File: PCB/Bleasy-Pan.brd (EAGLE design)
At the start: 33.6 x 62.2 mm, 14 parts, among them IC1 ATMEGA328-PU, Q1 8 MHz

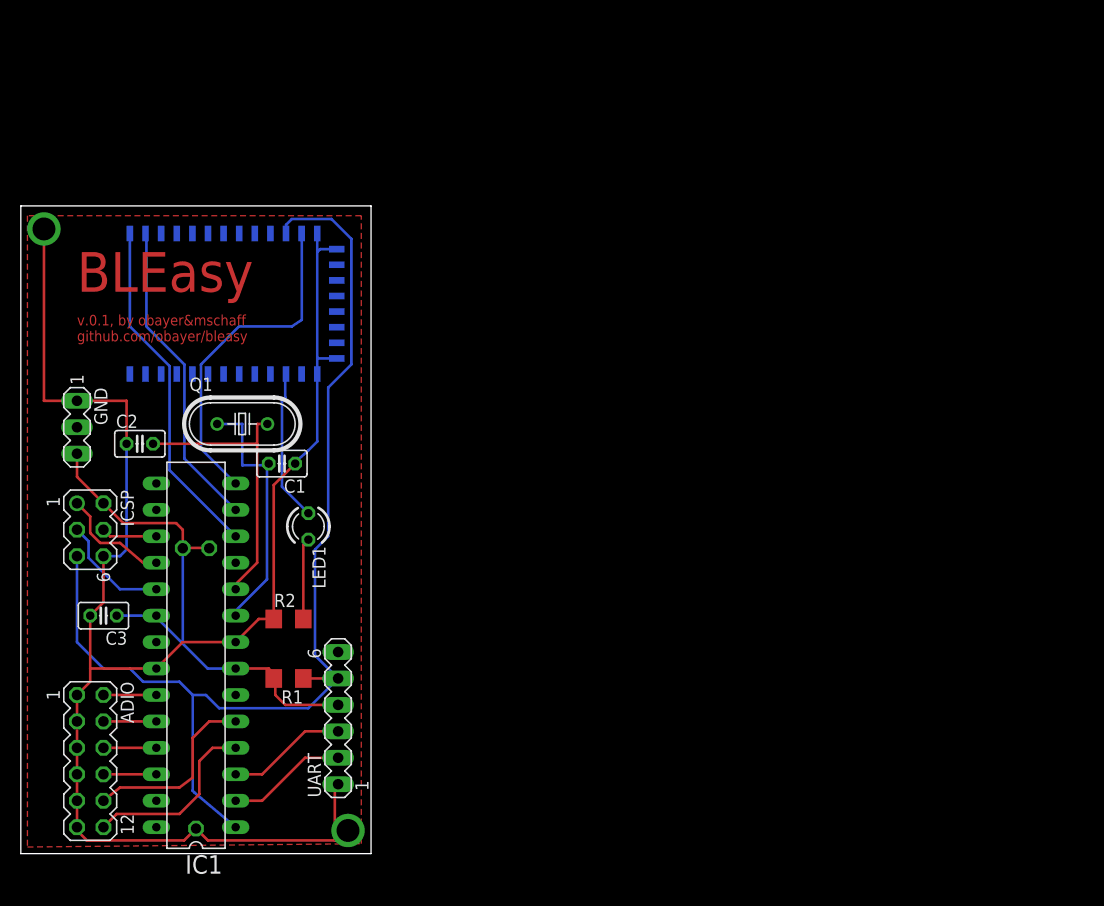
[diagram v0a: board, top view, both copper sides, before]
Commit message: feat(Panelize): Added panelized board.
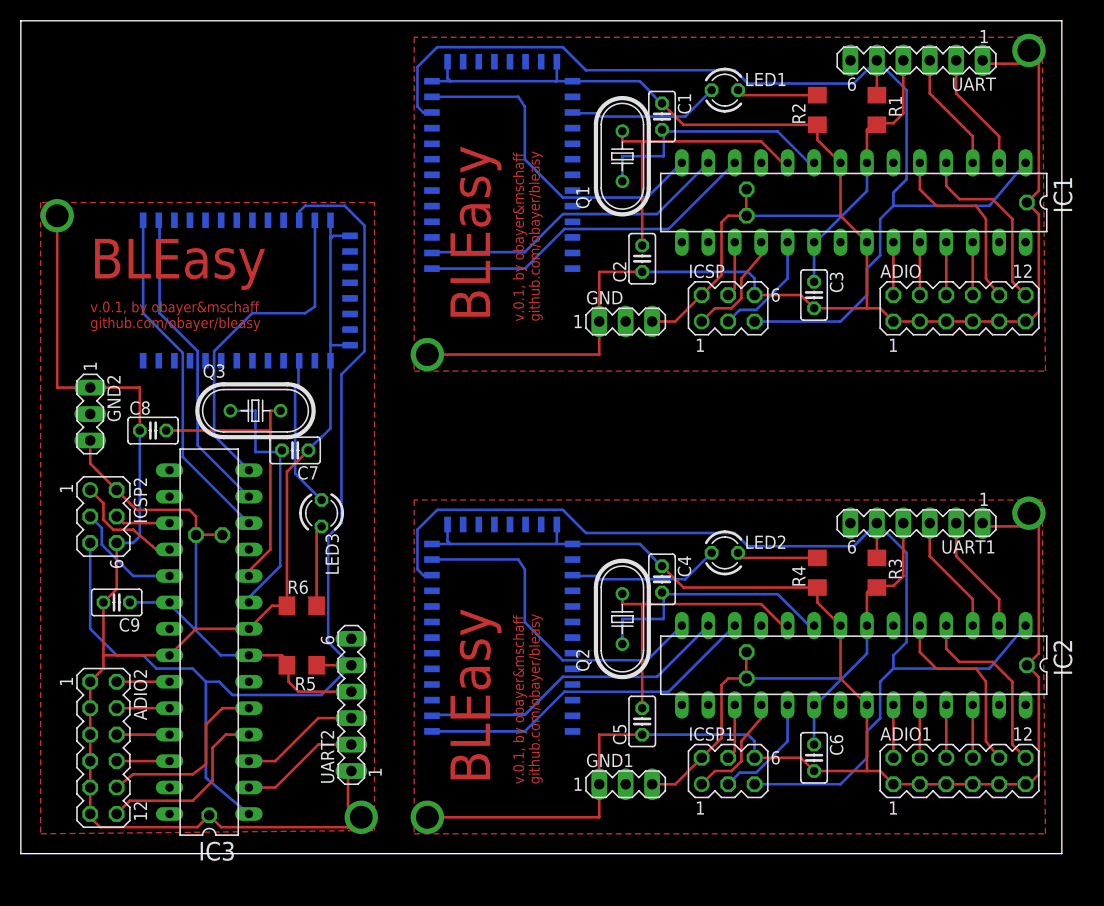
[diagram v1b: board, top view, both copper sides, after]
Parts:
- added ADIO1, ADIO2: (no value), con-lstb:MA06-2
- added BAT1, BAT3: CR2032_2+_1-SKT, con_bat_2032__s_:CR2032-SOCKET-THT
- added C4, C5, C7, C8: 22p, rcl:C025-025X050
- added C6, C9: 100n, rcl:C025-025X050
- added E2, E3: HM-10-BOARD, JNHuaMao:26.9X13X2.2_BOARD
- added GND1, GND2: (no value), con-lstb:MA03-1
- added IC2, IC3: ATMEGA328-PU, ATMEGA328P:DIL28-3
- added ICSP1, ICSP2: (no value), con-lstb:MA03-2
- added LED2, LED3: (no value), led:LED3MM
- added Q2, Q3: 8 MHz, crystal:HC49U70
- added R3, R5: 100k, resistor:R1206
- added R4, R6: 270, resistor:R1206
- added UART1, UART2: \, con-lstb:MA06-1
- moved ADIO 94.2 mm to (90.2, 52.4), turned to 0 degrees
- moved UART 84.1 mm to (86.0, 76.2), turned to 180 degrees
- moved BAT2 81.1 mm to (83.2, 62.5), turned to 0 degrees
- moved R1 78.6 mm to (82.2, 71.4), turned to 270 degrees
- moved IC1 76.7 mm to (80.0, 62.5), turned to 180 degrees
- moved C3 74.9 mm to (76.2, 53.7), turned to 270 degrees
- moved R2 70.5 mm to (76.5, 71.4), turned to 90 degrees
- moved ICSP 64.9 mm to (67.9, 52.4), turned to 0 degrees
- moved LED1 57.9 mm to (67.6, 73.3), turned to 0 degrees
- moved GND 53.7 mm to (58.1, 51.1), turned to 0 degrees
- moved C2 51.4 mm to (59.7, 57.1), turned to 90 degrees
- moved C1 49.4 mm to (61.6, 70.8), turned to 270 degrees
- moved Q1 44.7 mm to (57.8, 67.0), turned to 90 degrees
- moved E1 36.7 mm to (47.0, 56.2), turned to 180 degrees
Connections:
- new net +3V1: BAT1.2, BAT1.3, C6.1, GND1.3, IC2.20, IC2.7, ICSP1.2, R3.2, UART1.4
- new net +3V2: BAT3.2, BAT3.3, C9.1, GND2.3, IC3.20, IC3.7, ICSP2.2, R5.2, UART2.4
- new net GND1: ADIO1.1, ADIO1.11, ADIO1.3, ADIO1.5, ADIO1.7, ADIO1.9, BAT1.1, C4.1, C5.1, C6.2, E2.13, E2.14, E2.21, E2.22, GND1.1, IC2.22, IC2.8, ICSP1.6, R4.1, UART1.1
- new net GND2: ADIO2.1, ADIO2.11, ADIO2.3, ADIO2.5, ADIO2.7, ADIO2.9, BAT3.1, C7.1, C8.1, C9.2, E3.13, E3.14, E3.21, E3.22, GND2.1, IC3.22, IC3.8, ICSP2.6, R6.1, UART2.1
- new net HM10_RX1: E2.2, IC2.13
- new net HM10_RX2: E3.2, IC3.13
- new net HM10_TX1: E2.1, IC2.12
- new net HM10_TX2: E3.1, IC3.12
- new net MISO1: IC2.18, ICSP1.1
- new net MISO2: IC3.18, ICSP2.1
- new net N$14: C5.2, IC2.10, Q2.2
- new net N$15: C4.2, IC2.9, Q2.1
- new net N$16: IC2.17, ICSP1.4
- new net N$17: E2.12, IC2.14
- new net N$18: E2.24, LED2.A
- new net N$19: LED2.K, R4.2
- new net N$20: E2.3, E2.4
- new net N$21: ADIO1.12, IC2.4
- new net N$22: ADIO1.10, IC2.5
- new net N$23: ADIO1.2, IC2.23
- new net N$24: ADIO1.4, IC2.24
- new net N$25: ADIO1.6, IC2.25
- new net N$26: ADIO1.8, IC2.26
- new net N$27: C8.2, IC3.10, Q3.2
- new net N$28: C7.2, IC3.9, Q3.1
- new net N$29: IC3.17, ICSP2.4
- new net N$30: E3.12, IC3.14
- new net N$31: E3.24, LED3.A
- new net N$32: LED3.K, R6.2
- new net N$33: E3.3, E3.4
- new net N$34: ADIO2.12, IC3.4
- new net N$35: ADIO2.10, IC3.5
- new net N$36: ADIO2.2, IC3.23
- new net N$37: ADIO2.4, IC3.24
- new net N$38: ADIO2.6, IC3.25
- new net N$39: ADIO2.8, IC3.26
- new net RST1: E2.11, IC2.1, ICSP1.5, R3.1, UART1.5
- new net RST2: E3.11, IC3.1, ICSP2.5, R5.1, UART2.5
- new net RX1: IC2.2, UART1.2
- new net RX2: IC3.2, UART2.2
- new net SCK1: IC2.19, ICSP1.3
- new net SCK2: IC3.19, ICSP2.3
- new net TX1: IC2.3, UART1.3
- new net TX2: IC3.3, UART2.3
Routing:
- net GND1: track 0.00 -> 164.3 mm, vias 0 -> 2
- net GND2: track 0.00 -> 164.3 mm, vias 0 -> 2
- net RST1: track 0.00 -> 107.8 mm
- net RST2: track 0.00 -> 107.8 mm
- net +3V2: track 0.00 -> 54.0 mm
- net +3V1: track 0.00 -> 54.0 mm
- net HM10_TX2: track 0.00 -> 33.3 mm
- net HM10_TX1: track 0.00 -> 33.3 mm
- net N$17: track 0.00 -> 32.5 mm
- net N$30: track 0.00 -> 32.5 mm
- net HM10_RX2: track 0.00 -> 30.1 mm
- net HM10_RX1: track 0.00 -> 30.1 mm
- net N$14: track 0.00 -> 27.7 mm
- net N$27: track 0.00 -> 27.7 mm
- net N$28: track 0.00 -> 24.7 mm
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- added copper zone on layer 1, net GND1
- added copper zone on layer 1, net GND2
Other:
- board size 33.6 x 62.2 mm -> 100 x 80 mm
- board text added: "ADIO"
- board text added: "BAT2"
- board text added: "C1"
- board text added: "C2"
- board text added: "C3"
- board text added: "E1"
- board text added: "GND"
- board text added: "IC1"
- board text added: "ICSP"
- board text added: "LED1"
- board text added: "Q1"
- board text added: "R1"
- board text added: "R2"
- board text added: "UART"
